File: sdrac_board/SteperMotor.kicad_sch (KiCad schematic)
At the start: 18 parts, among them J4 STEPER_DRIVER_CONTROL, J5 STEPER_DRIVER_MOTOR_OUT, U7 SN74LV1T34DBV, U8 SN74LV1T34DBV, U9 SN74LV1T34DBV

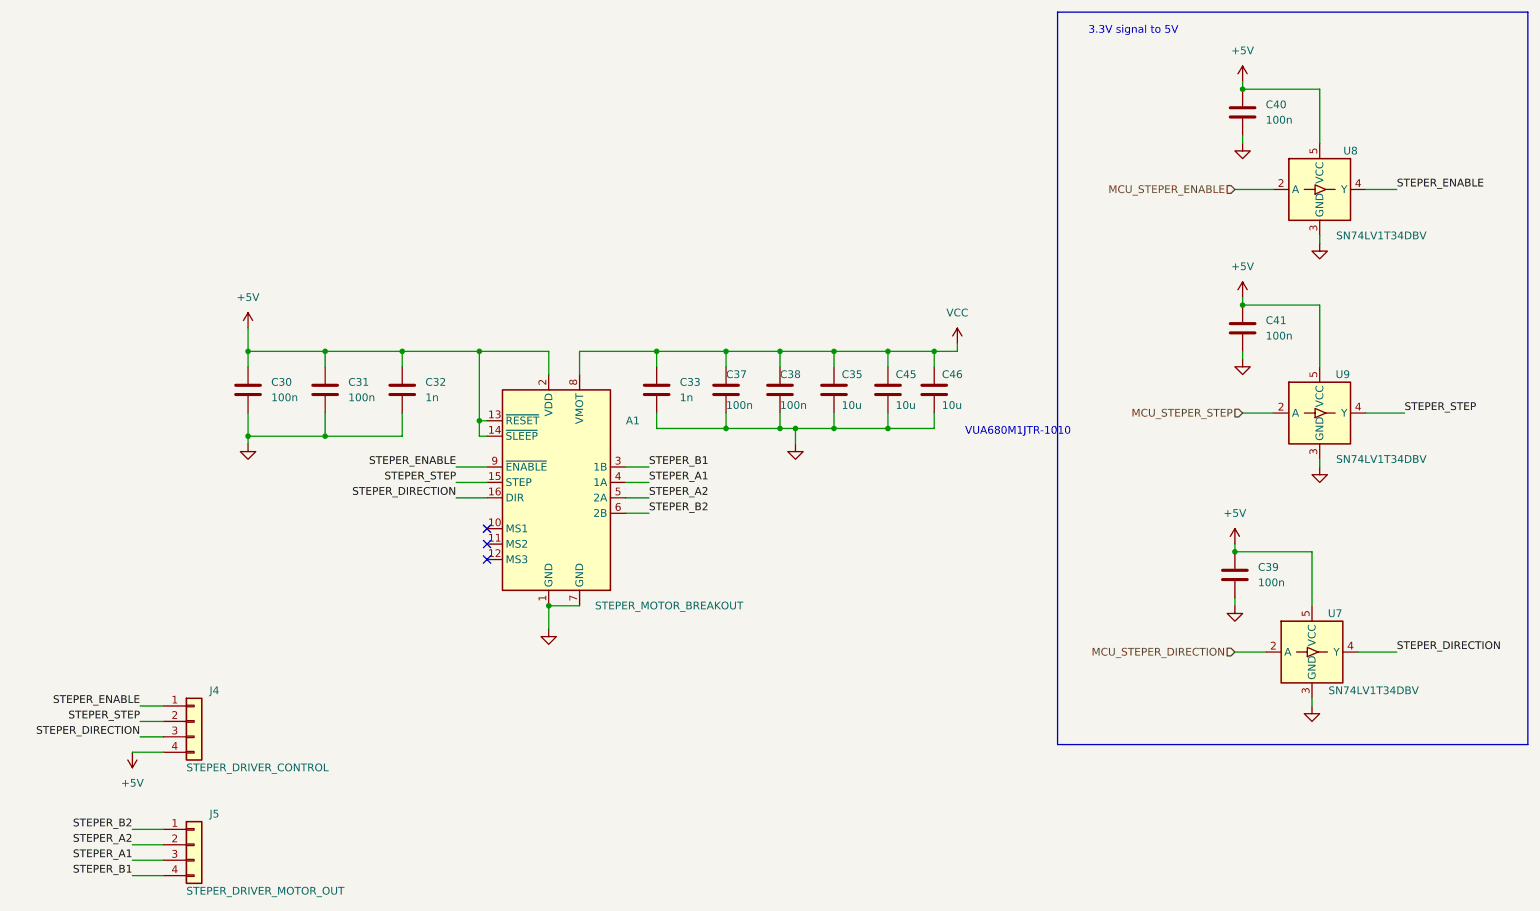
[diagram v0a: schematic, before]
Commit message: added second I2C communscation lane for synchronization and added wyas to change mcirosteping with resistors
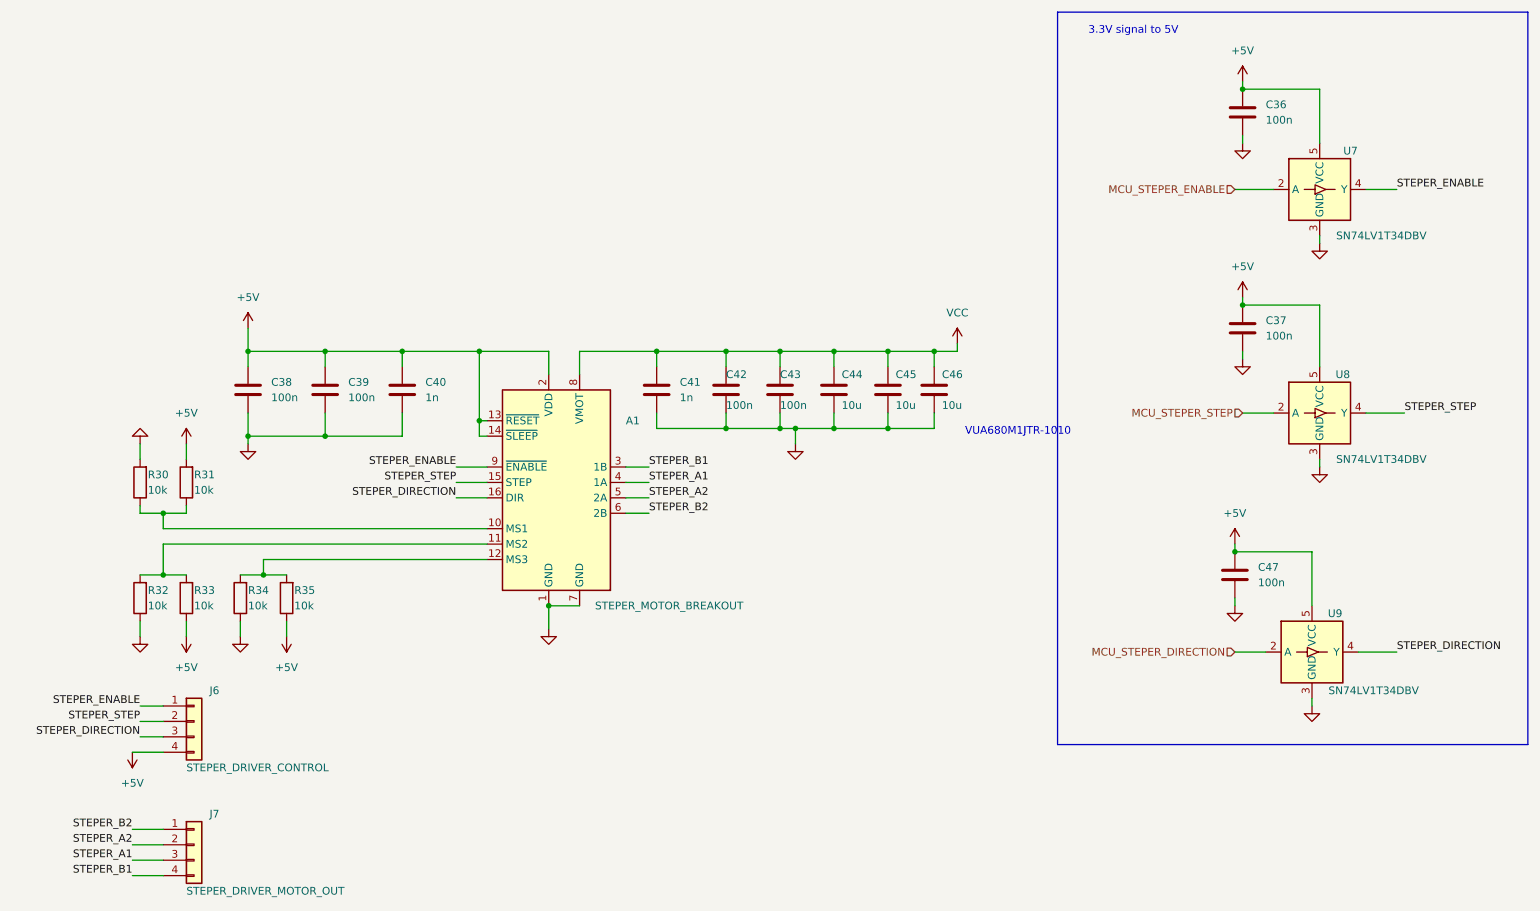
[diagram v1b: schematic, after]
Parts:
- added R30, R31, R32, R33, R34, R35: 10k, Resistor_SMD:R_0402_1005Metric, symbol Device:R
- renumbered C40 to C36, C41 to C37, C30 to C38, C31 to C39, C32 to C40, C33 to C41, C37 to C42, C38 to C43, C35 to C44, C39 to C47, J4 to J6, J5 to J7, U8 to U7, U9 to U8, U7 to U9
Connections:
- net +5V: now also R31.2, R33.1, R35.1
- net GND: now also R30.2, R32.1, R34.1
- net at A1.10 (MS1): now also R30.1, R31.1
- net at A1.11 (MS2): now also R32.2, R33.2
- net at A1.12 (MS3): now also R34.2, R35.2
- no-connect marks 3 -> 0

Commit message: added hardware address selector
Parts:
- renumbered R30 to R36, R31 to R37, R32 to R38, R33 to R39, R34 to R40, R35 to R41

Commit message: added 10A screw terminal
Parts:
- renumbered C36 to C37, C37 to C38, C38 to C39, C39 to C40, C40 to C41, C41 to C42, C42 to C43, C43 to C44, C44 to C45, C45 to C46, C46 to C47, C47 to C48, J6 to J7, J7 to J8
